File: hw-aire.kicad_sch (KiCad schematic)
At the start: 54 parts, among them J1 Conn_01x02_Pin, J2 Screw_Terminal_01x02, J3 Screw_Terminal_01x12, J4 Conn_01x04_Pin, K1 JRC-21F(4100), K2 JRC-21F(4100), K3 JRC-21F(4100), Q1 2N2219, Q2 2N2219, Q3 2N2219, Q4 2N2219, SW1 SW_Push, SW2 SW_Push, U1 HLK-2M05, U2 NCP1117-3.3_SOT223, U3 ESP-12E, U4 SHT4x, U5 BMP581

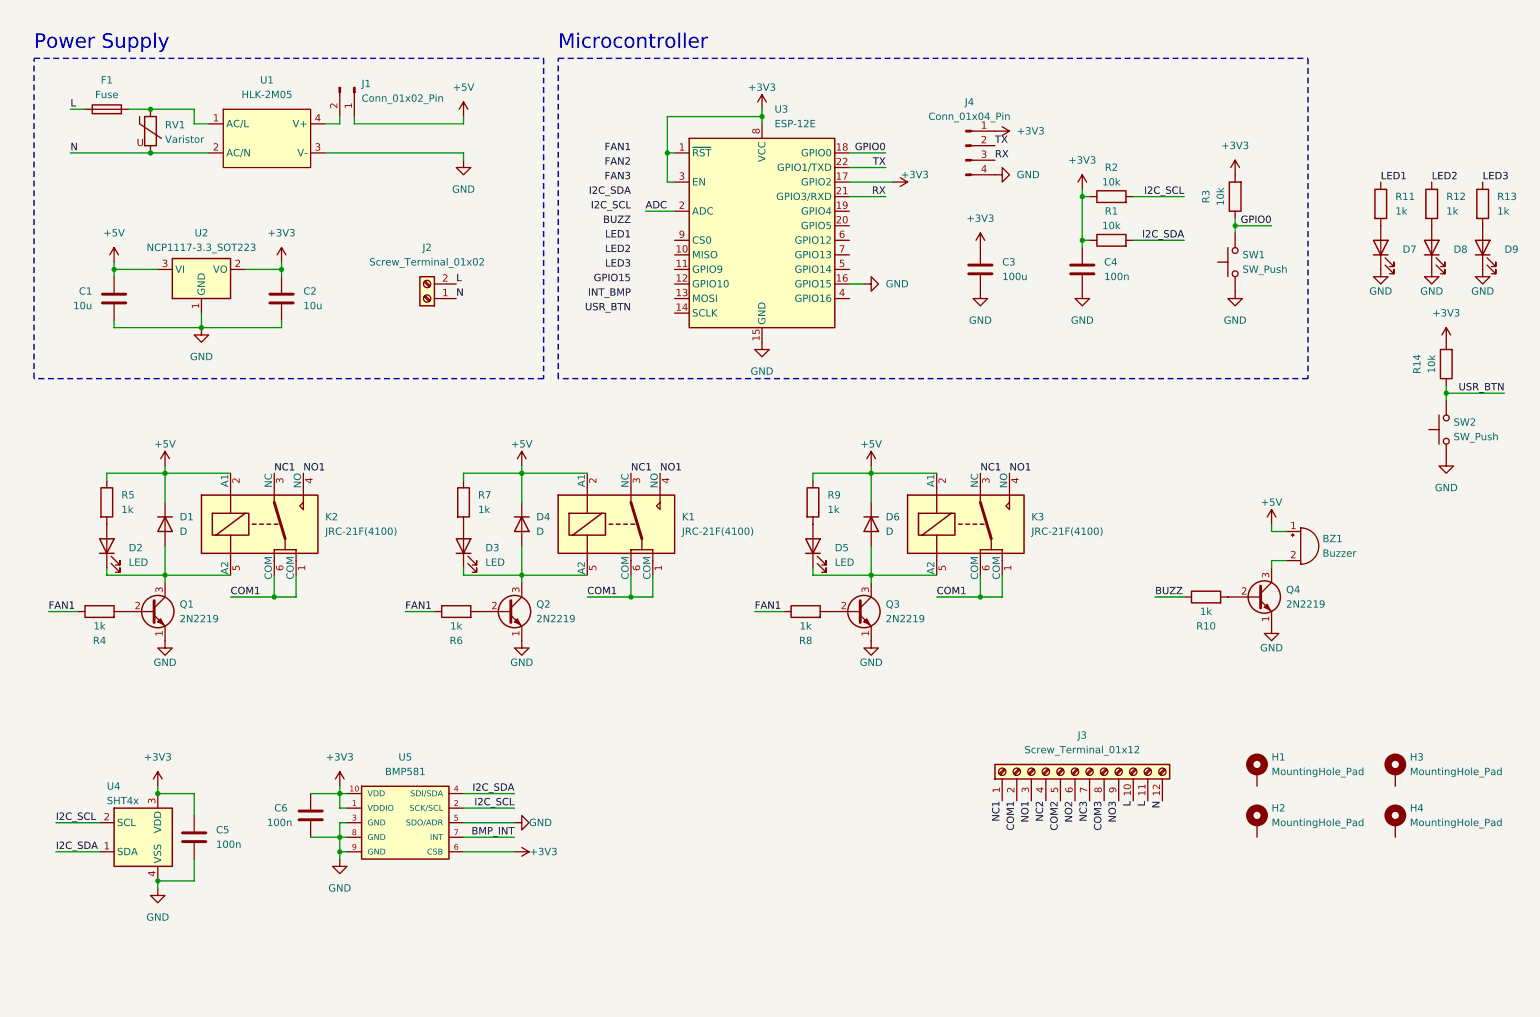
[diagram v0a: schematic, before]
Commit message: All components linked with fp in schematic
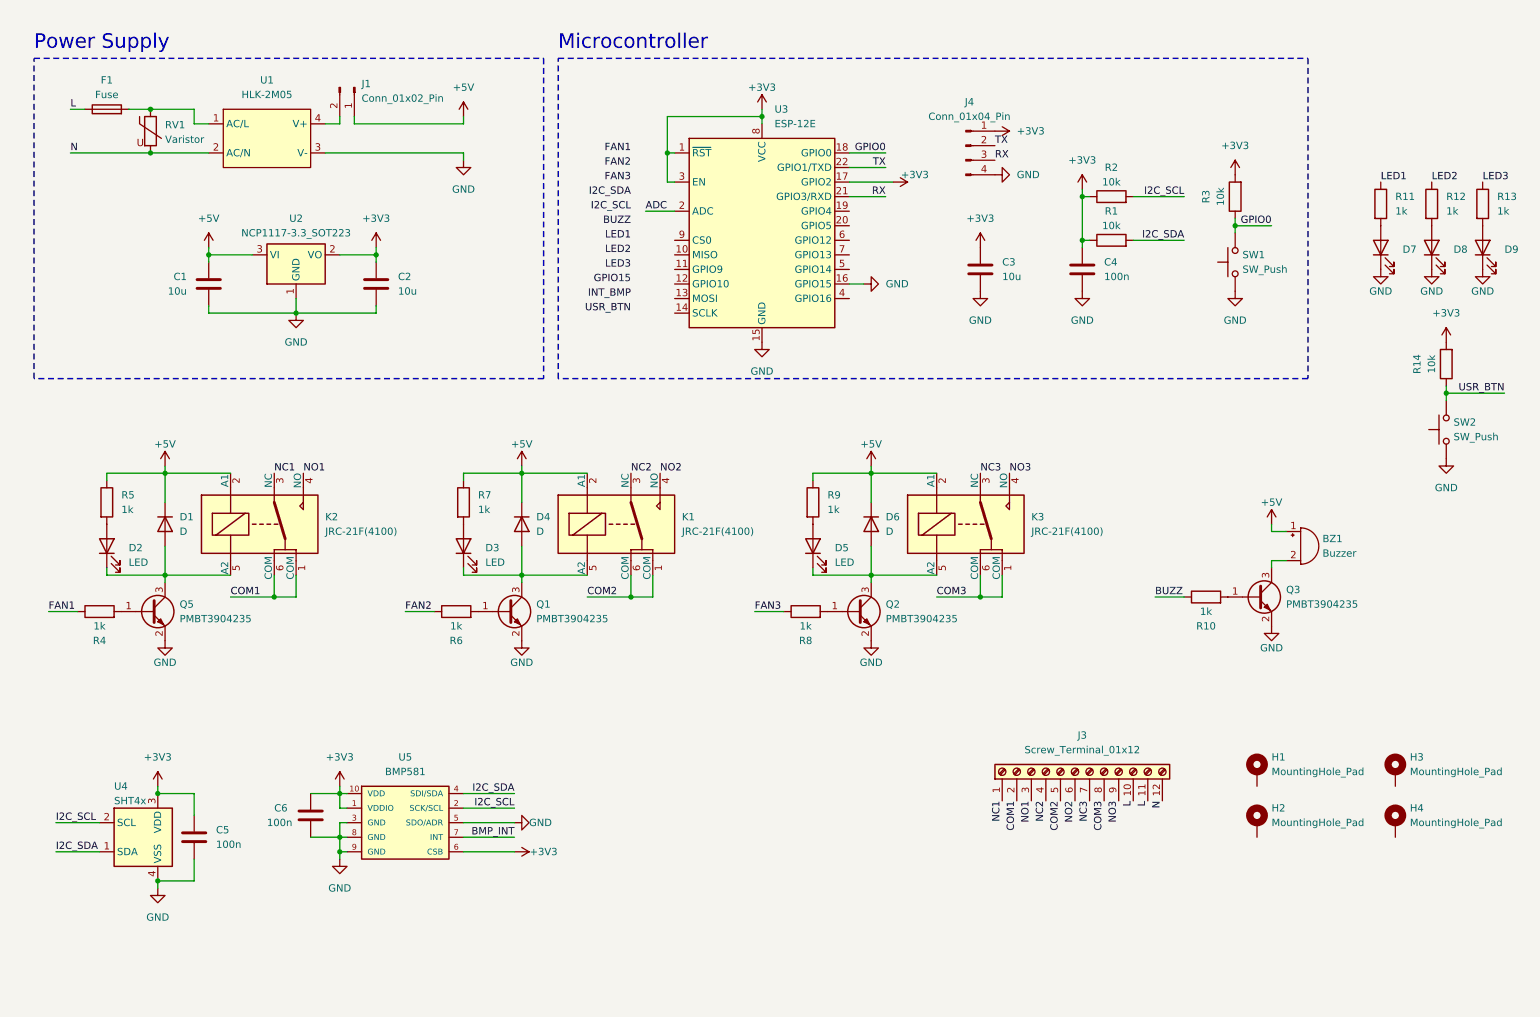
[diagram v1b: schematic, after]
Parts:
- removed J2: Screw_Terminal_01x02, symbol Connector:Screw_Terminal_01x02
- removed Q1, Q2, Q3, Q4: 2N2219, Package_TO_SOT_THT:TO-39-3, symbol Transistor_BJT:2N2219
- removed U4: SHT4x, Sensor_Humidity:Sensirion_DFN-4_1.5x1.5mm_P0.8mm_SHT4x_NoCentralPad, symbol Sensor_Humidity:SHT4x
- added Q1, Q2, Q3, Q5: PMBT3904235, Package_TO_SOT_SMD:SOT-23, symbol guille-lib:PMBT3904235
- added U4: SHT4x, guille-lib:SHT4x, symbol guille-lib:SHT4x
- BZ1: footprint (none) -> Buzzer_Beeper:Buzzer_12x9.5RM7.6
- C1, C2: footprint (none) -> Capacitor_SMD:C_1206_3216Metric
- C3: value 100u -> 10u; footprint (none) -> Capacitor_SMD:C_1206_3216Metric
- C4, C5, C6: footprint (none) -> Capacitor_SMD:C_0402_1005Metric
- D1, D4, D6, SW2: footprint (none) -> Diode_SMD:D_SOD-323
- D2, D3, D5: footprint (none) -> LED_SMD:LED_0402_1005Metric
- D7, D8, D9: footprint (none) -> LED_THT:LED_D3.0mm
- F1: footprint (none) -> guille-lib:Fuse_2512_6332Metric
- H1, H2, H3, H4: footprint (none) -> MountingHole:MountingHole_3.2mm_M3_Pad_TopBottom
- J1: footprint (none) -> Connector_PinHeader_2.54mm:PinHeader_1x02_P2.54mm_Vertical
- J3: footprint (none) -> TerminalBlock_Phoenix:TerminalBlock_Phoenix_MKDS-1,5-12-5.08_1x12_P5.08mm_Horizontal
- J4: footprint (none) -> Connector_PinHeader_2.54mm:PinHeader_1x04_P2.54mm_Vertical
- R1, R10, R11, R12, R13, R14, R2, R3, R4, R5, R6, R7, R8, R9: footprint (none) -> Resistor_SMD:R_0402_1005Metric
- RV1: footprint (none) -> Varistor:RV_Disc_D12mm_W4.5mm_P7.5mm
- SW1: footprint (none) -> guille-lib:SW_SPST_PTS810
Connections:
- net +3V3: now also U4.3 (VDD)
- net COM1: no longer K1.1 (COM), K1.6 (COM), K3.1 (COM), K3.6 (COM)
- net COM2: now also K1.1 (COM), K1.6 (COM)
- net COM3: now also K3.1 (COM), K3.6 (COM)
- net FAN1: no longer R6.1, R8.1
- net FAN2: now also R6.1
- net FAN3: now also R8.1
- net GND: now also Q1.2, Q2.2, Q3.2, Q5.2, U4.4 (VSS)
- net I2C_SCL: now also U4.2 (SCL)
- net I2C_SDA: now also U4.1 (SDA)
- net NC1: no longer K1.3 (NC), K3.3 (NC)
- net NC2: now also K1.3 (NC)
- net NC3: now also K3.3 (NC)
- net NO1: no longer K1.4 (NO), K3.4 (NO)
- net NO2: now also K1.4 (NO)
- net NO3: now also K3.4 (NO)
- net at D5.1 (K), D6.2 (A), K3.5 (A2): now also Q2.3
- net at R10.2: now also Q3.1
- net at BZ1.2 (+): now also Q3.3
- net at R6.2: now also Q1.1
- net at D3.1 (K), D4.2 (A), K1.5 (A2): now also Q1.3
- net at R4.2: now also Q5.1
- net at D1.2 (A), D2.1 (K), K2.5 (A2): now also Q5.3
- net at R8.2: now also Q2.1
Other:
- moved on the sheet: C1, C2, U2

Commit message: Update schematic
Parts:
- added JP1, JP2, JP3: SolderJumper_2_Open, Jumper:SolderJumper-2_P1.3mm_Open_TrianglePad1.0x1.5mm, symbol Jumper:SolderJumper_2_Open
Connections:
- net BMP_INT: now also U3.4 (GPIO16)
- net BUZZ: now also U3.13 (MOSI)
- net COM1: now also JP1.2 (B)
- net COM2: now also JP2.2 (B)
- net COM3: now also JP3.2 (B)
- net FAN1: now also U3.10 (MISO)
- net FAN2: now also U3.11 (GPIO9)
- net FAN3: now also U3.12 (GPIO10)
- net GND: now also H1.1, H2.1, H3.1, H4.1
- net I2C_SCL: now also U3.7 (GPIO13)
- net I2C_SDA: now also U3.5 (GPIO14)
- net LED1: now also U3.6 (GPIO12)
- net LED2: now also U3.20 (GPIO5)
- net LED3: now also U3.19 (GPIO4)
- net USR_BTN: now also U3.14 (SCLK)
- net LF: now reaches F1.2, RV1.1, U1.1 (AC/L)
- net LF: now also JP1.1 (A), JP2.1 (A), JP3.1 (A)
- net ADC: no longer names the net of U3.2 (ADC)
- no-connect marks 0 -> 2
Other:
- note added: "Check ADC and CB0"
- note added: "Environment"
- note added: "IN/OUT"
- company: (none) -> Guillermo González
- title: (none) -> Aire
- moved on the sheet: BZ1, C1, C2, C3, C4, C5, C6, D7, D8, D9, F1, H1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

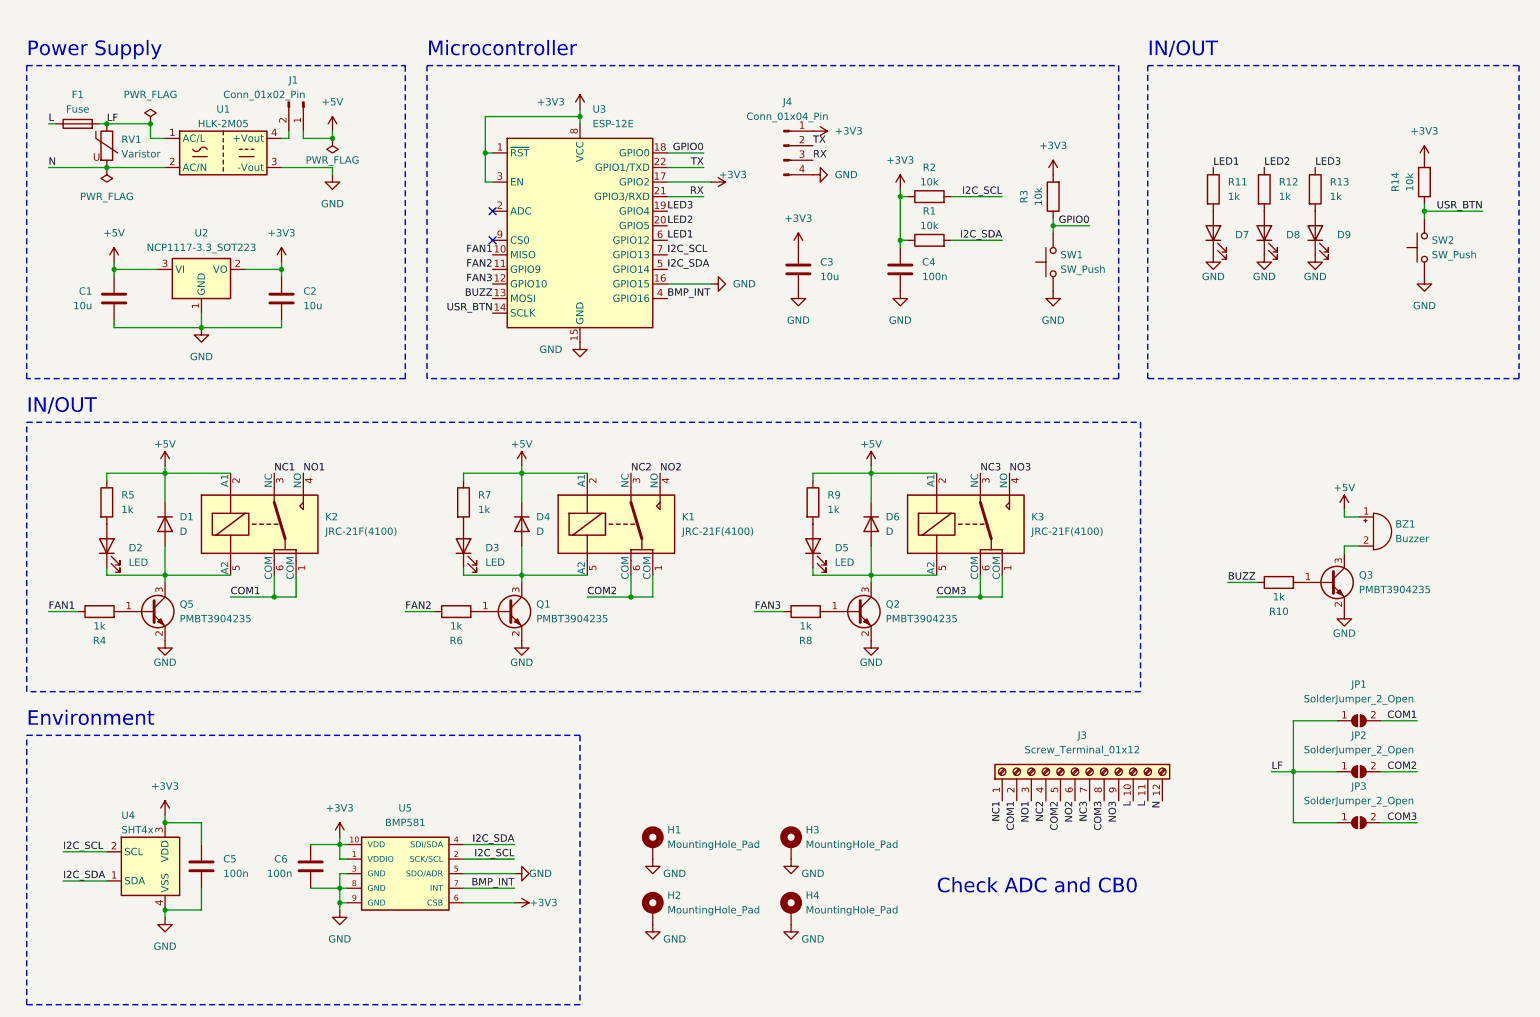
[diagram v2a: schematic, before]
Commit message: Sch changes, add net classes and first placement
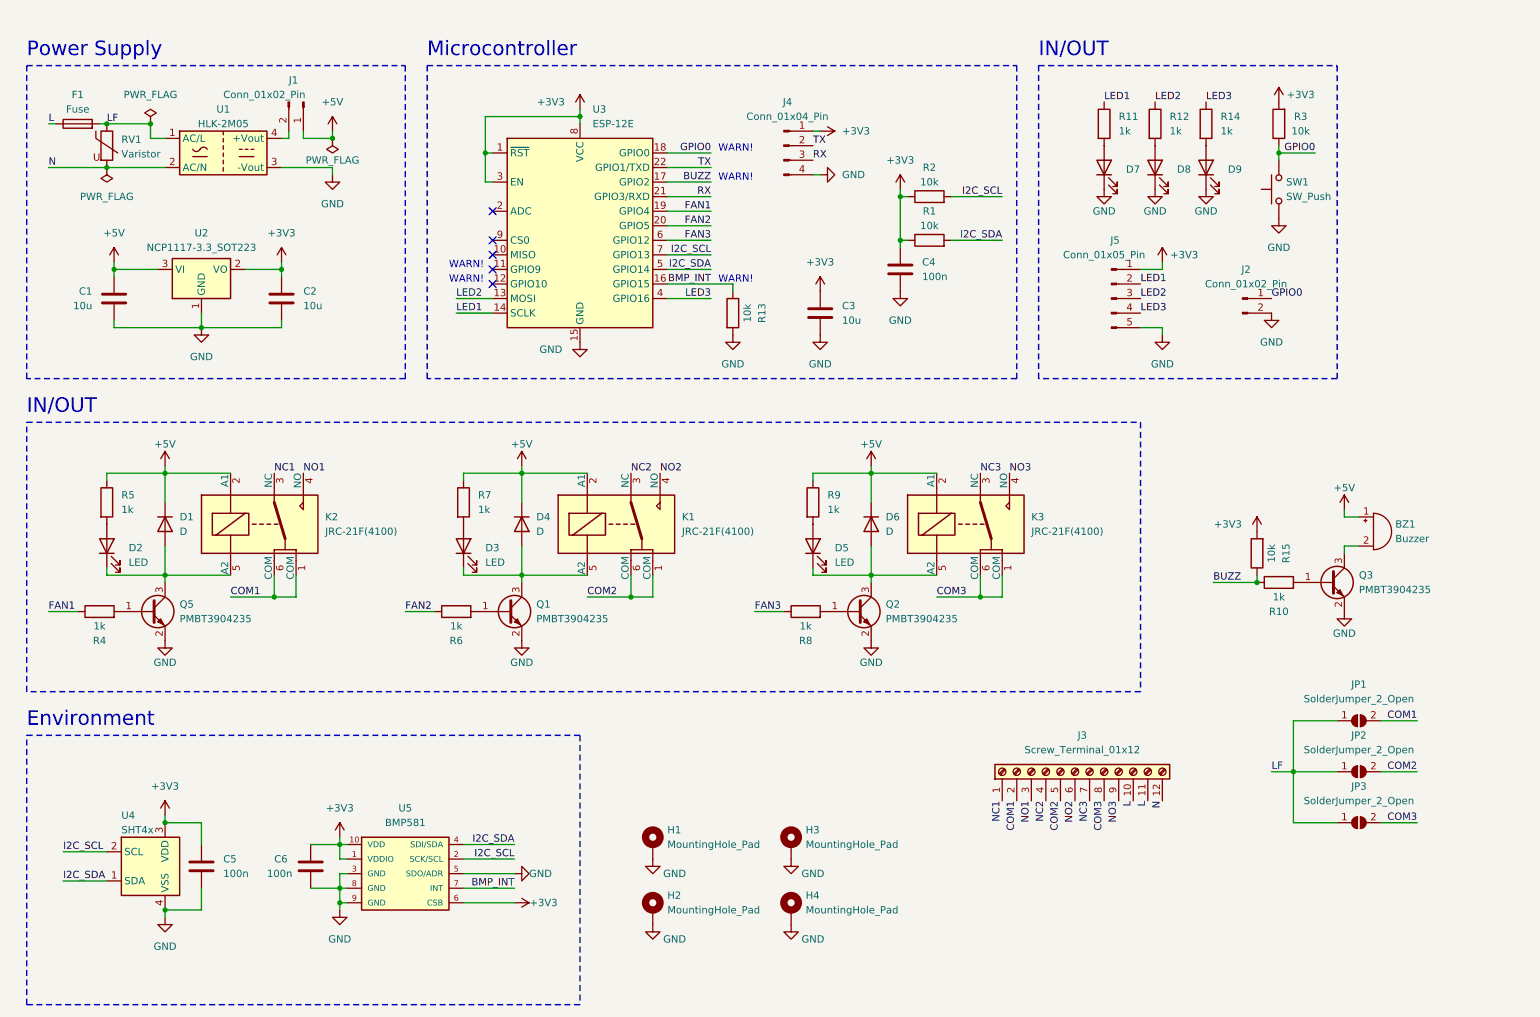
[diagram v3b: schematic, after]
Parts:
- removed SW2: SW_Push, Diode_SMD:D_SOD-323, symbol Switch:SW_Push
- added J2: Conn_01x02_Pin, Connector_PinHeader_2.54mm:PinHeader_1x02_P2.54mm_Vertical, symbol Connector:Conn_01x02_Pin
- added J5: Conn_01x05_Pin, Connector_PinHeader_2.54mm:PinHeader_1x05_P2.54mm_Vertical, symbol Connector:Conn_01x05_Pin
- added R15: 10k, Resistor_SMD:R_0402_1005Metric, symbol Device:R
- R13: value 1k -> 10k
- R14: value 10k -> 1k
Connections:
- net +3V3: now also J5.1 (Pin_1), R15.2; no longer R14.2, U3.17 (GPIO2)
- net BMP_INT: now also R13.1, U3.16 (GPIO15); no longer U3.4 (GPIO16)
- net BUZZ: now also U3.17 (GPIO2), R15.1; no longer U3.13 (MOSI)
- net FAN1: now also U3.19 (GPIO4); no longer U3.10 (MISO)
- net FAN2: now also U3.20 (GPIO5); no longer U3.11 (GPIO9)
- net FAN3: now also U3.6 (GPIO12); no longer U3.12 (GPIO10)
- net GND: now also R13.2, J2.2 (Pin_2), J5.5 (Pin_5); no longer U3.16 (GPIO15)
- net GPIO0: now also J2.1 (Pin_1)
- net LED1: now also U3.14 (SCLK), J5.2 (Pin_2); no longer U3.6 (GPIO12)
- net LED2: now also U3.13 (MOSI), J5.3 (Pin_3); no longer U3.20 (GPIO5)
- net LED3: now also R14.1, U3.4 (GPIO16), J5.4 (Pin_4); no longer R13.1, U3.19 (GPIO4)
- net at D9.2 (A): now also R14.2; no longer R13.2
- removed net USR_BTN: R14.1, U3.14 (SCLK)
- no-connect marks 2 -> 5
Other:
- note added: "WARN!"
- note removed: "Check ADC and CB0"
- moved on the sheet: C3, D7, D8, R11, R12, R3, SW1
